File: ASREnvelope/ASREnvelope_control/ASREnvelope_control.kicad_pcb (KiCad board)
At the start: 2 copper layers, 20 x 100 mm, 19 parts, among them J1 GATE, J3 OUT, J4 INV OUT, J5 Conn_01x06_Male, J6 Conn_01x04_Male, SW1 SW_SPDT

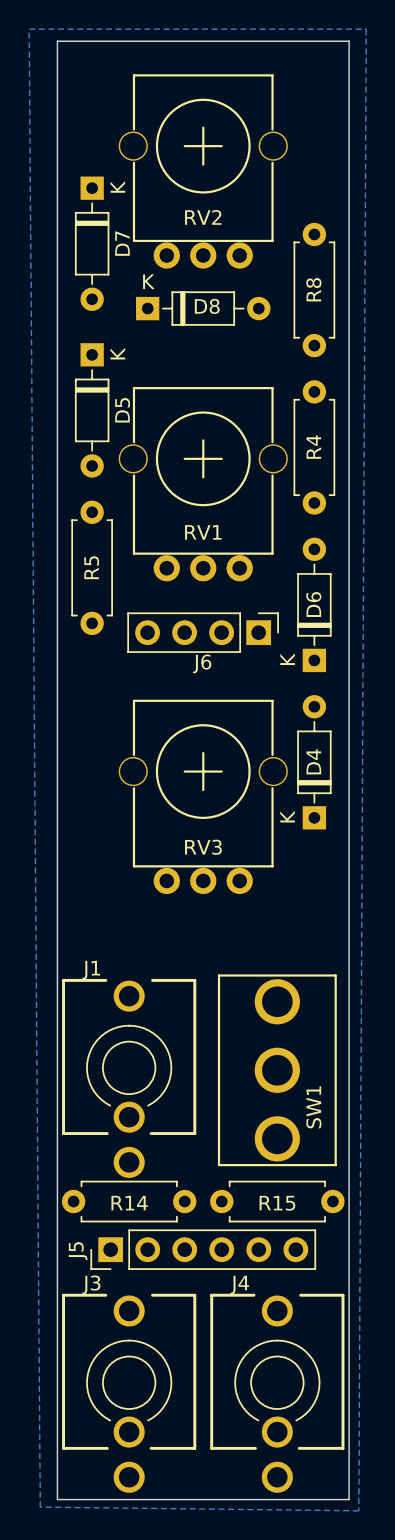
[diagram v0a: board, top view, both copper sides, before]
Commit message: finish control traces
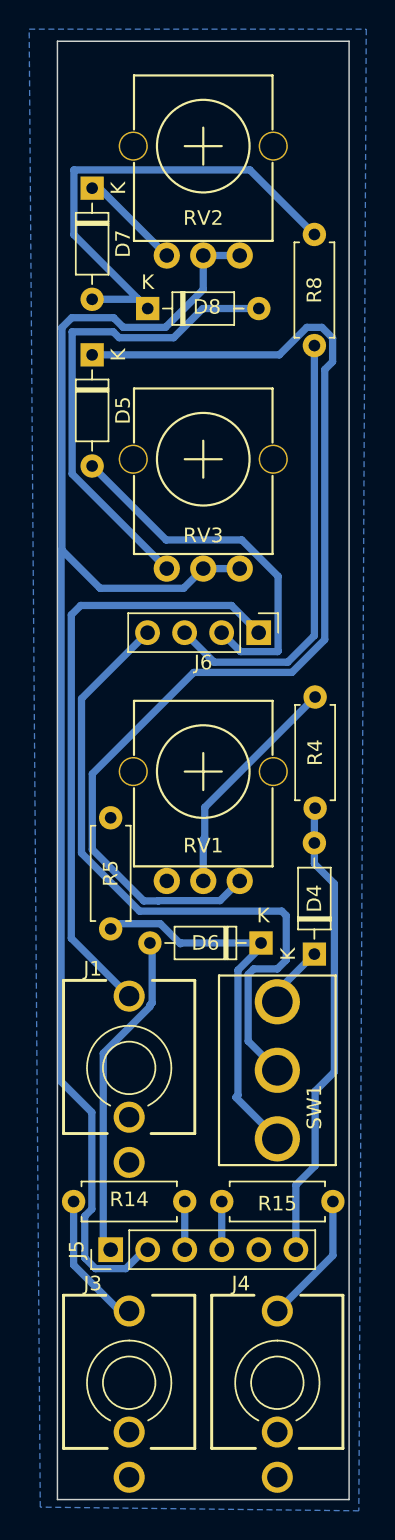
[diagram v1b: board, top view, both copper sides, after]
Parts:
- moved RV1 21.4 mm to (151.1, 94.5)
- moved RV3 21.4 mm to (151.1, 73.1)
- moved R5 21.0 mm to (144.8, 105.3)
- moved R4 20.9 mm to (158.8, 97.0)
- moved D6 19.7 mm to (155.1, 106.2), turned to 180 degrees
- moved D4 9.34 mm to (158.8, 107.0)
- moved R14 7.62 mm to (149.9, 124.0), turned to 180 degrees
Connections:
- J1 pad S: GroundA -> GND
- J1 pad TN: GroundA -> GND
- J3 pad S: GroundA -> GND
- J4 pad S: GroundA -> GND
- J5 pad 1: GateJackA -> Switch1A
- J5 pad 2: OutJackA -> Conn3A
- J5 pad 3: InvOutJackA -> OutJackA
- J5 pad 4: Switch1A -> InvOutJackA
- J5 pad 5: Switch2A -> GND
- J6 pad 1: Conn1A -> GateJackA
- J6 pad 2: GroundA -> Conn1A
- J6 pad 3: Conn3A -> Conn2A
- J6 pad 4: Conn4A -> Switch2A
- R5 pad 2: GroundA -> GND
- R8 pad 2: Conn3A -> Conn2A
- RV1 pad 1: GroundA -> GND
- RV2 pad 1: Conn4A -> Net-(D7-Pad1)
- RV2 pad 2: Conn4A -> Conn3A
- RV2 pad 3: Net-(D7-Pad1) -> Conn3A
- RV3 pad 1: Conn4A -> Net-(D8-Pad2)
- RV3 pad 2: Conn4A -> Conn3A
- RV3 pad 3: Net-(D8-Pad2) -> Conn3A
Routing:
- net Conn3A: track 0.00 -> 100.2 mm
- net Net-(D5-Pad1): track 0.00 -> 75.5 mm
- net Switch2A: track 0.00 -> 46.3 mm
- net GateJackA: track 0.00 -> 41.7 mm
- net Net-(D7-Pad2): track 0.00 -> 34.0 mm
- net Net-(D8-Pad2): track 0.00 -> 32.7 mm
- net Switch3A: track 0.00 -> 32.0 mm
- net Conn2A: track 0.00 -> 30.4 mm
- net Net-(D6-Pad1): track 0.00 -> 26.4 mm
- net Conn1A: track 0.00 -> 25.4 mm
- net Switch1A: track 0.00 -> 22.7 mm
- net Net-(R4-Pad2): track 0.00 -> 15.8 mm
- net Net-(J3-PadT): track 0.00 -> 9.47 mm
- net Net-(J4-PadT): track 0.00 -> 9.08 mm
- net Net-(D7-Pad1): track 0.00 -> 7.03 mm
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- added copper zone on B.Cu, net GND
- removed copper zone on B.Cu, net GroundA
